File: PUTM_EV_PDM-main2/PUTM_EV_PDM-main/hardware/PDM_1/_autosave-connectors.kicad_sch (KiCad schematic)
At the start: 4 parts, among them J2 UPT-08-01-01-L-RA, J5 UPT-02-01-01-X-RA, J6 Conn_01x06, J7 UPT-08-01-01-L-RA

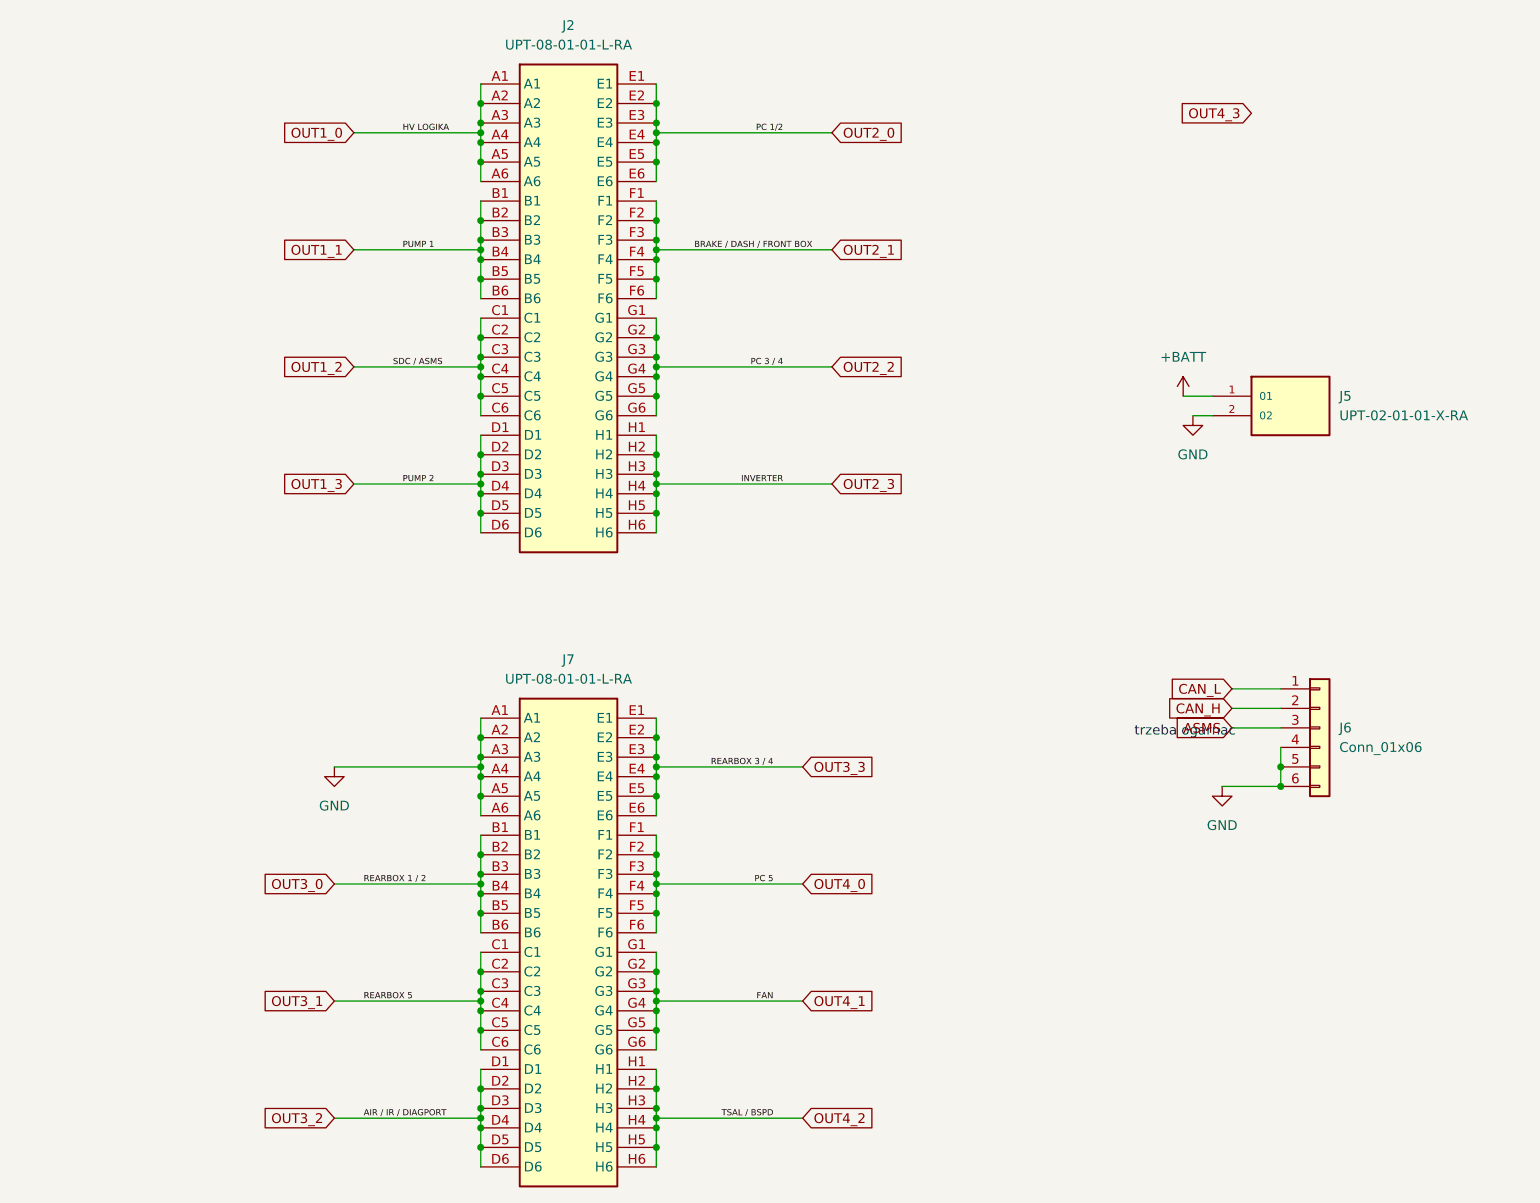
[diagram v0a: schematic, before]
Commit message: Koniec połączeń sygnałów
Wszystkie sygnały z stm poprowadzone
Zmienione ułożenie połączeń do złącz
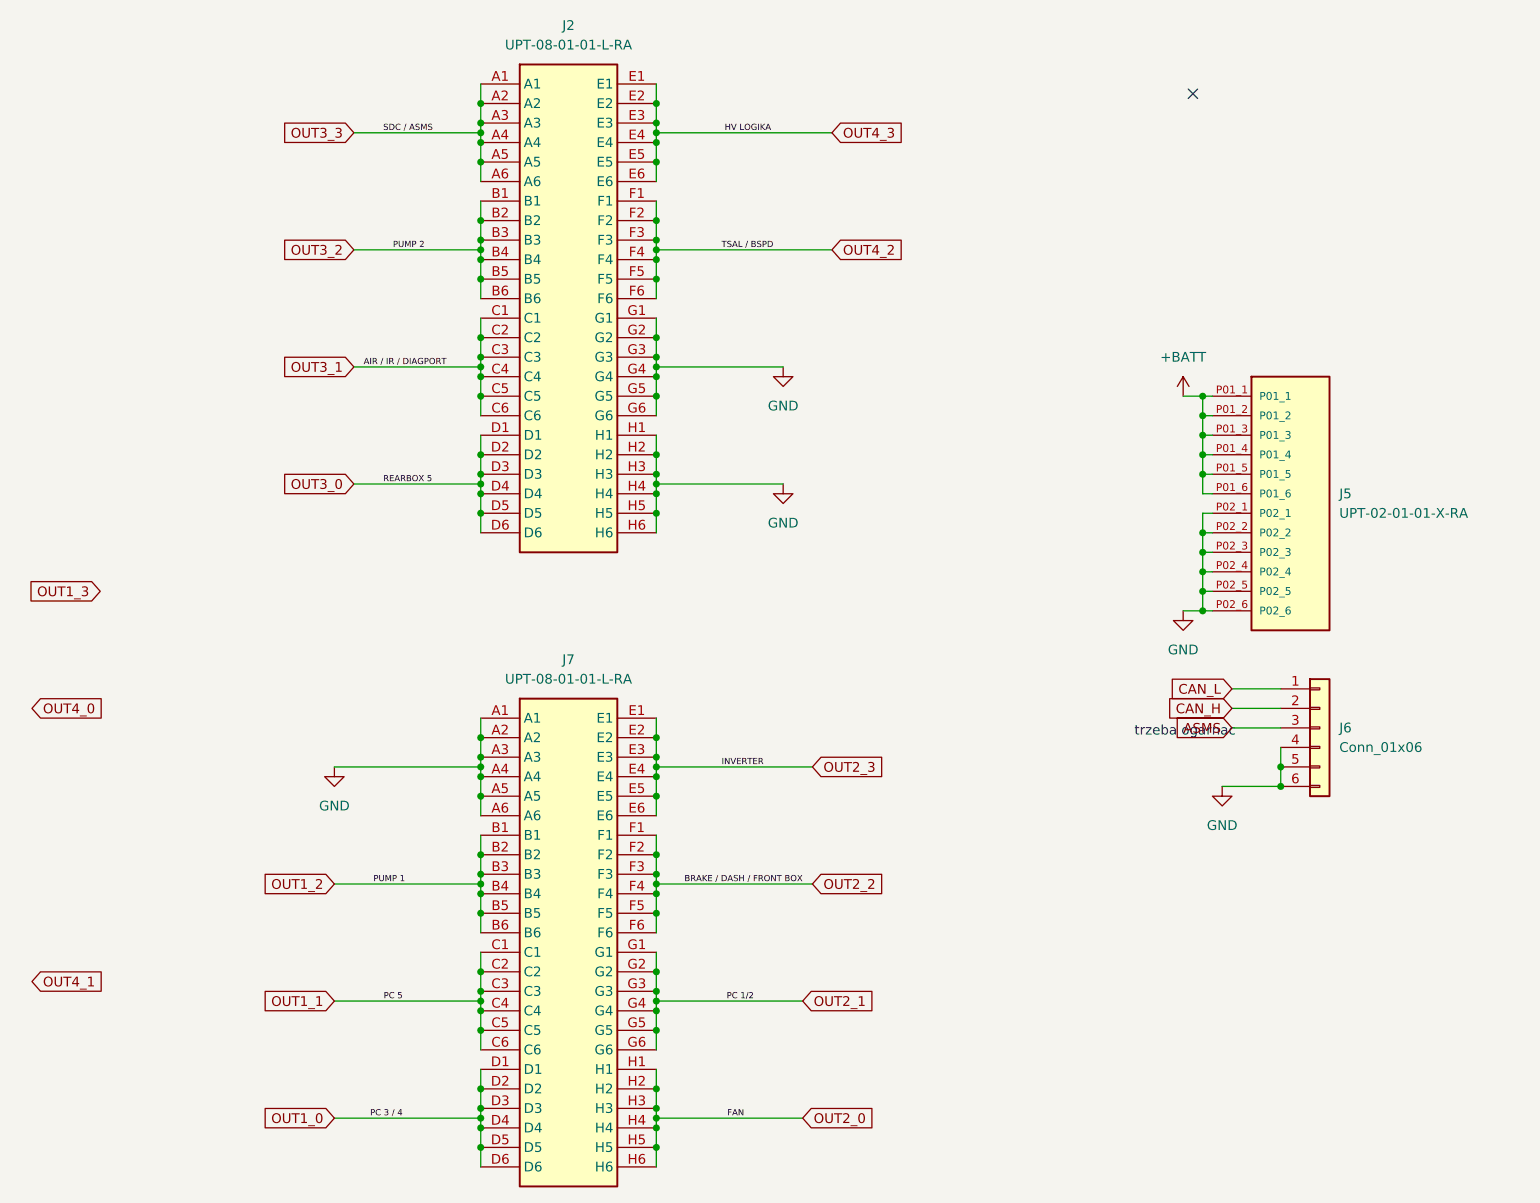
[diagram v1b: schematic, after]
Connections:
- net +BATT: now also J5.P01_1, J5.P01_2, J5.P01_3, J5.P01_4, J5.P01_5, J5.P01_6; no longer J5.1 (01)
- net GND: now also J2.G1, J2.G2, J2.G3, J2.G4, J2.G5, J2.G6, J2.H1, J2.H2, J2.H3, J2.H4, J2.H5, J2.H6, J5.P02_1, J5.P02_2, J5.P02_3, J5.P02_4, J5.P02_5, J5.P02_6; no longer J5.2 (02)
- net OUT1_0: now also J7.D1, J7.D2, J7.D3, J7.D4, J7.D5, J7.D6; no longer J2.A1, J2.A2, J2.A3, J2.A4, J2.A5, J2.A6
- net OUT1_1: now also J7.C1, J7.C2, J7.C3, J7.C4, J7.C5, J7.C6; no longer J2.B1, J2.B2, J2.B3, J2.B4, J2.B5, J2.B6
- net OUT1_2: now also J7.B1, J7.B2, J7.B3, J7.B4, J7.B5, J7.B6; no longer J2.C1, J2.C2, J2.C3, J2.C4, J2.C5, J2.C6
- net OUT1_3: no longer J2.D1, J2.D2, J2.D3, J2.D4, J2.D5, J2.D6
- net OUT2_0: now also J7.H1, J7.H2, J7.H3, J7.H4, J7.H5, J7.H6; no longer J2.E1, J2.E2, J2.E3, J2.E4, J2.E5, J2.E6
- net OUT2_1: now also J7.G1, J7.G2, J7.G3, J7.G4, J7.G5, J7.G6; no longer J2.F1, J2.F2, J2.F3, J2.F4, J2.F5, J2.F6
- net OUT2_2: now also J7.F1, J7.F2, J7.F3, J7.F4, J7.F5, J7.F6; no longer J2.G1, J2.G2, J2.G3, J2.G4, J2.G5, J2.G6
- net OUT2_3: now also J7.E1, J7.E2, J7.E3, J7.E4, J7.E5, J7.E6; no longer J2.H1, J2.H2, J2.H3, J2.H4, J2.H5, J2.H6
- net OUT3_0: now also J2.D1, J2.D2, J2.D3, J2.D4, J2.D5, J2.D6; no longer J7.B1, J7.B2, J7.B3, J7.B4, J7.B5, J7.B6
- net OUT3_1: now also J2.C1, J2.C2, J2.C3, J2.C4, J2.C5, J2.C6; no longer J7.C1, J7.C2, J7.C3, J7.C4, J7.C5, J7.C6
- net OUT3_2: now also J2.B1, J2.B2, J2.B3, J2.B4, J2.B5, J2.B6; no longer J7.D1, J7.D2, J7.D3, J7.D4, J7.D5, J7.D6
- net OUT3_3: now also J2.A1, J2.A2, J2.A3, J2.A4, J2.A5, J2.A6; no longer J7.E1, J7.E2, J7.E3, J7.E4, J7.E5, J7.E6
- net OUT4_0: no longer J7.F1, J7.F2, J7.F3, J7.F4, J7.F5, J7.F6
- net OUT4_1: no longer J7.G1, J7.G2, J7.G3, J7.G4, J7.G5, J7.G6
- net OUT4_2: now also J2.F1, J2.F2, J2.F3, J2.F4, J2.F5, J2.F6; no longer J7.H1, J7.H2, J7.H3, J7.H4, J7.H5, J7.H6
- net OUT4_3: now also J2.E1, J2.E2, J2.E3, J2.E4, J2.E5, J2.E6
- no-connect marks 0 -> 1
